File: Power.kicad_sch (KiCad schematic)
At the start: 25 parts, among them U201 AP62200WU-7, U202 TLV75733PDRV

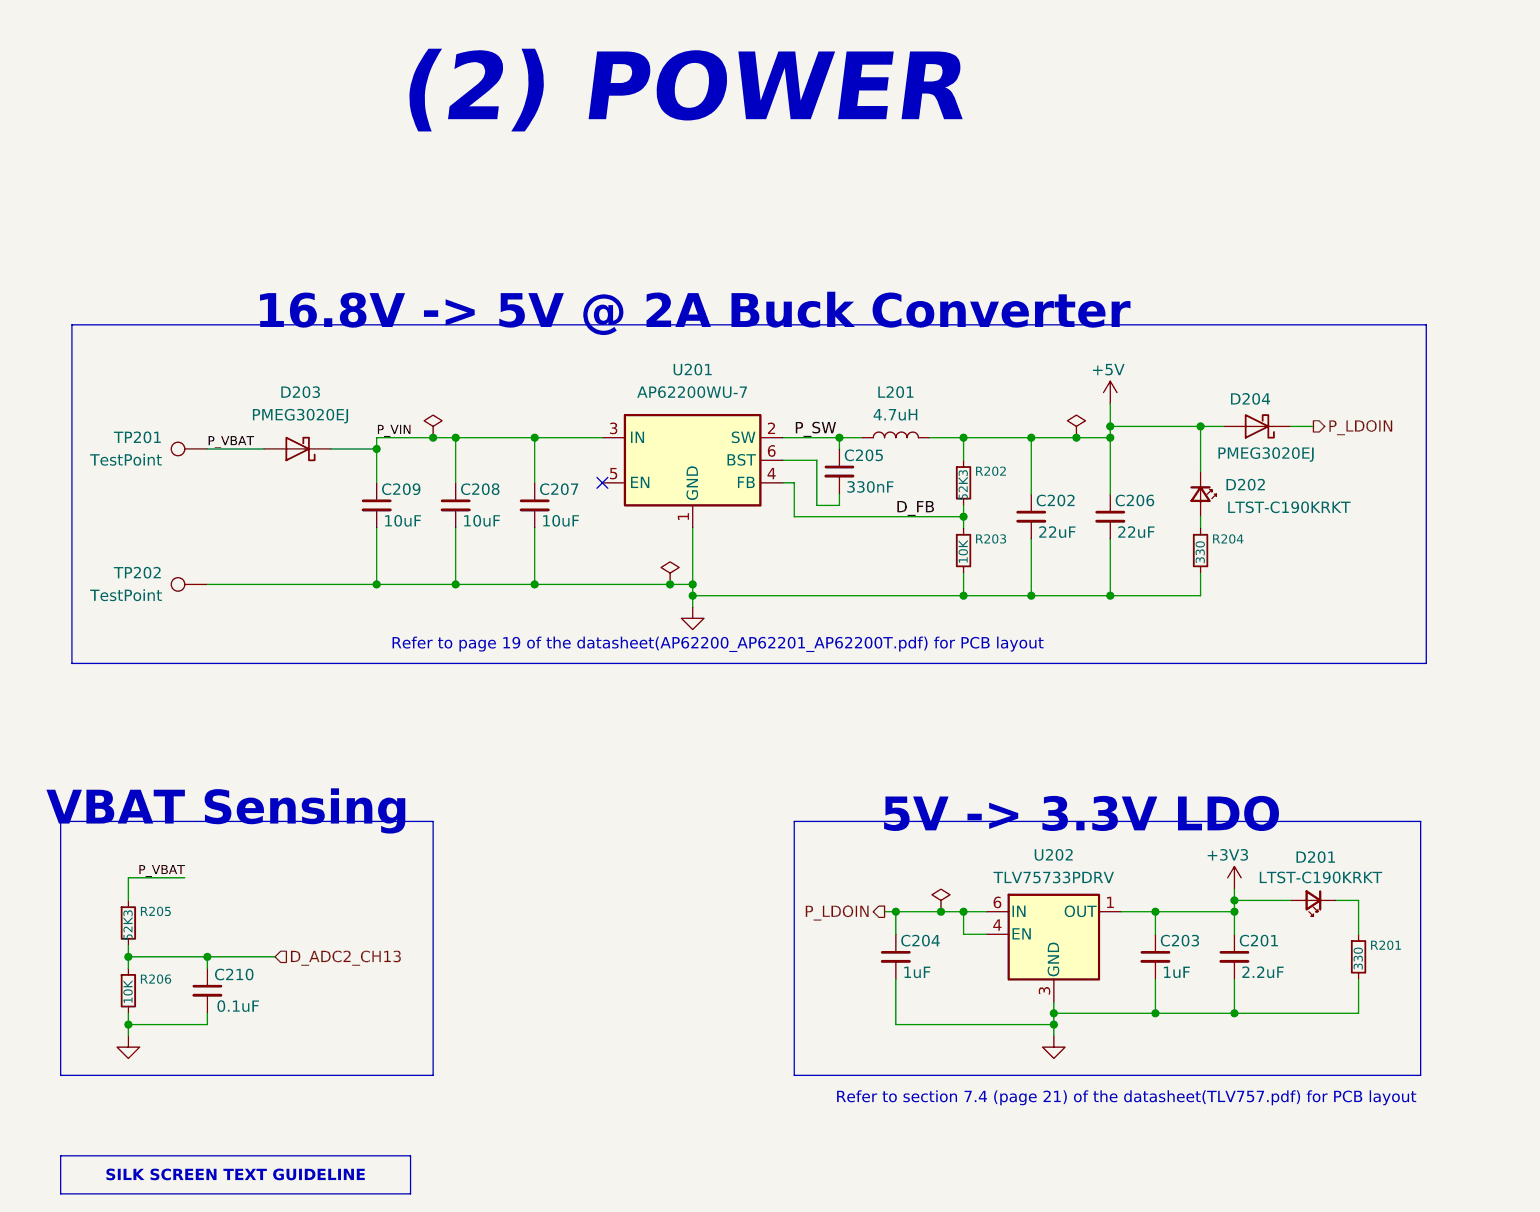
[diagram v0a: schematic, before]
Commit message: refactor: change tim5 ch 1 label to ch 2
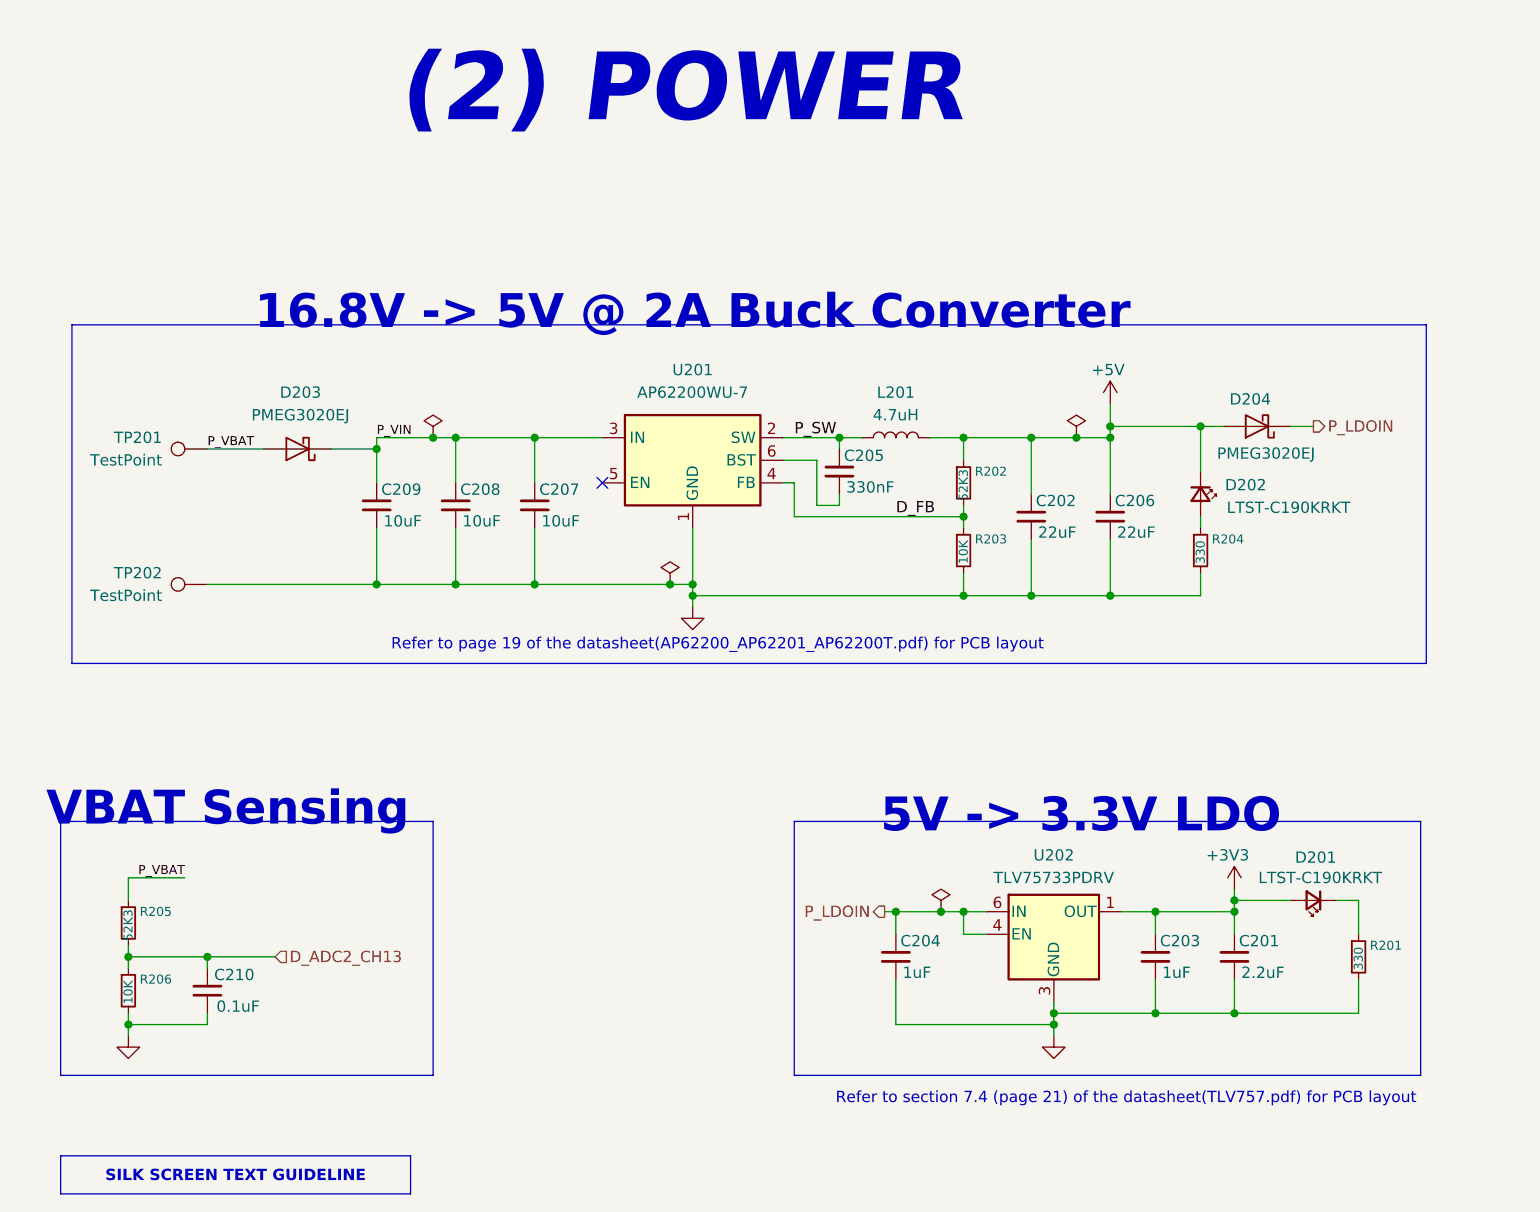
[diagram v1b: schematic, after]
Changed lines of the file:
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@@
 		)
 		(property "Description" "Unpolarized capacitor, small symbol"
-			(at 111.76 76.2 0)
+			(at 111.76 86.36 0)
 			(hide yes)
 			(show_name no)
@@
 		)
 		(property "Description" "Unpolarized capacitor, small symbol"
-			(at 120.65 76.2 0)
+			(at 120.65 86.36 0)
 			(hide yes)
 			(show_name no)
@@
 		)
 		(property "Description" "Unpolarized capacitor, small symbol"
-			(at 208.28 127 0)
+			(at 208.28 137.16 0)
 			(hide yes)
 			(show_name no)
@@
 		)
 		(property "Description" "Unpolarized capacitor, small symbol"
-			(at 170.18 127 0)
+			(at 170.18 137.16 0)
 			(hide yes)
 			(show_name no)
@@
 		)
 		(property "Description" "Unpolarized capacitor, small symbol"
-			(at 92.71 130.81 0)
+			(at 92.71 140.97 0)
 			(hide yes)
 			(show_name no)
@@
 		)
 		(property "Description" "Unpolarized capacitor, small symbol"
-			(at 129.54 76.2 0)
+			(at 129.54 86.36 0)
 			(hide yes)
 			(show_name no)
@@
 		)
 		(property "Description" "Unpolarized capacitor, small symbol"
-			(at 185.42 77.47 0)
+			(at 185.42 87.63 0)
 			(hide yes)
 			(show_name no)
@@
 		)
 		(property "Description" "Unpolarized capacitor, small symbol"
-			(at 199.39 127 0)
+			(at 199.39 137.16 0)
 			(hide yes)
 			(show_name no)
@@
 		)
 		(property "Description" "Unpolarized capacitor, small symbol"
-			(at 194.31 77.47 0)
+			(at 194.31 87.63 0)
 			(hide yes)
 			(show_name no)
@@
 		)
 		(property "Description" "Unpolarized capacitor, small symbol"
-			(at 163.83 72.39 0)
+			(at 163.83 82.55 0)
 			(hide yes)
 			(show_name no)
